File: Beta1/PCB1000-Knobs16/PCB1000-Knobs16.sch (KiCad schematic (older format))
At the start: 33 parts, among them U1000 MCP3008T-I/SL, U2 MCP3008T-I/SL

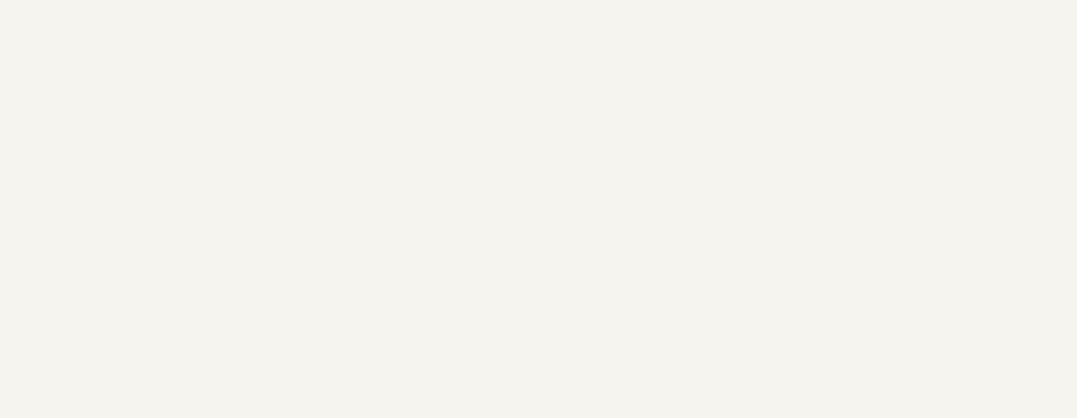
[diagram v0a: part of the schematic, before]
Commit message: Increased width by 2U. Ready for FAB
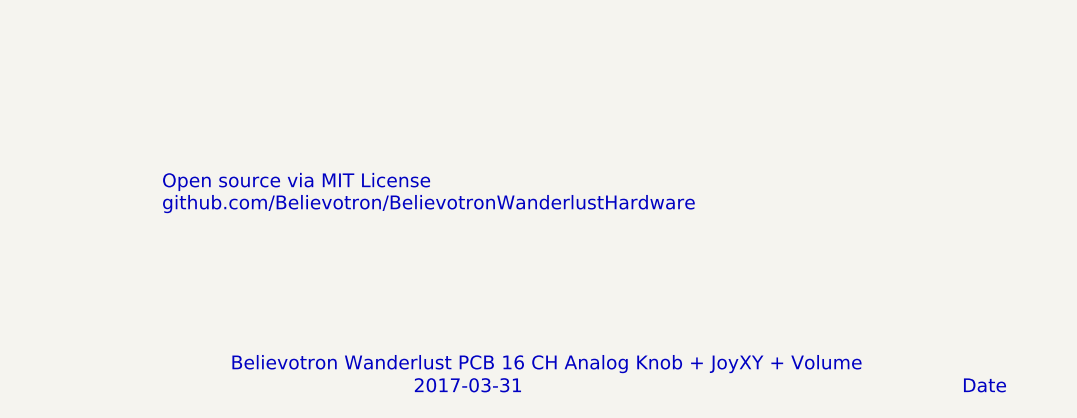
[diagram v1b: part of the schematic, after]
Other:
- note added: "2017-03-31"
- note added: "Believotron Wanderlust PCB 16 CH Analog Knob + JoyXY + Volume"
- note added: "Date"
- note added: "\nOpen source via MIT License\ngithub.com/Believotron/BelievotronWanderlustHardware"
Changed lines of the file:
@@
 LIBS:Zilog
 LIBS:believotron_wanderlust
-LIBS:Knobs-cache
 EELAYER 25 0
 EELAYER END
@@
 Wire Wire Line
 	5350 8650 5550 8650
+Text Notes 13450 10350 0    60   ~ 0
+2017-03-31
+Text Notes 12650 10250 0    60   ~ 0
+Believotron Wanderlust PCB 16 CH Analog Knob + JoyXY + Volume
+Text Notes 12350 9550 0    60   ~ 0
+\nOpen source via MIT License\ngithub.com/Believotron/BelievotronWanderlustHardware
+Text Notes 15850 10350 0    60   ~ 0
+Date
 $EndSCHEMATC
